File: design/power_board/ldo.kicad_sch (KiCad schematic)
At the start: 10 parts, among them U2 LM317M_DCY

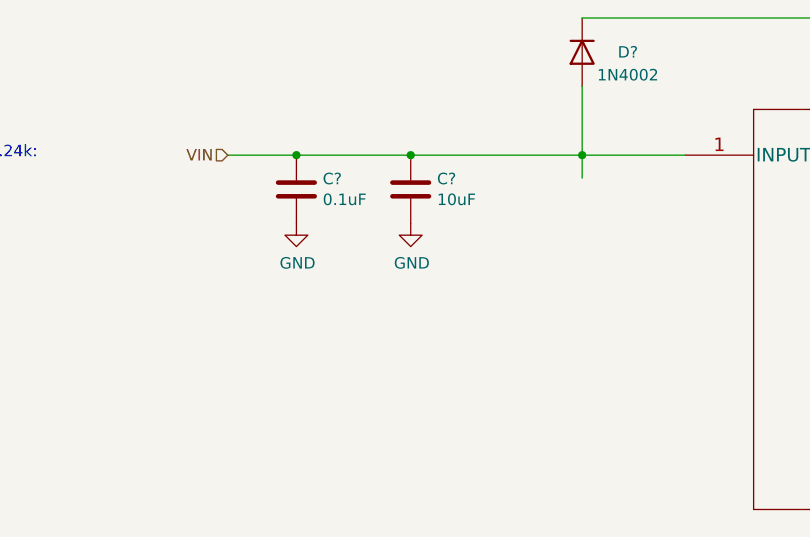
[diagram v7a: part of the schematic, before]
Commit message: Added LED
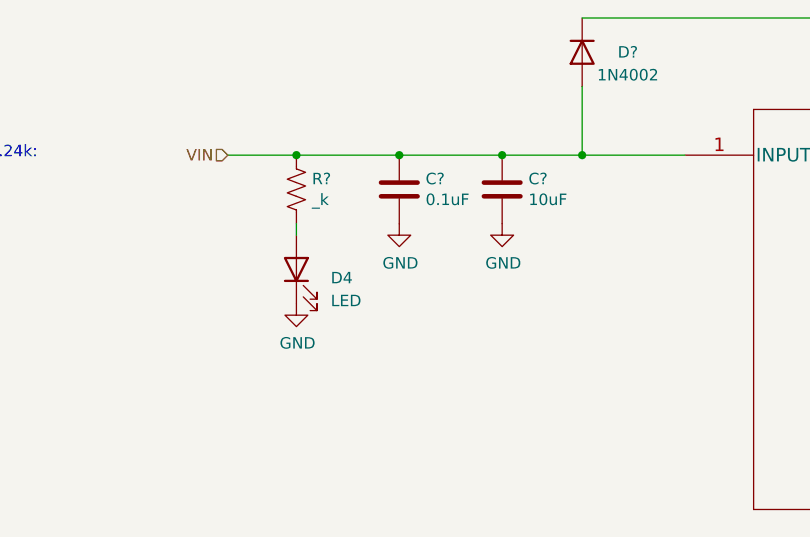
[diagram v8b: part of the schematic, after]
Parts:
- added D4: LED, symbol Device:LED
- added R?: _k, Resistor_SMD:R_0805_2012Metric_Pad1.20x1.40mm_HandSolder, symbol Device:R_US
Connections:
- net GND: now also D4.1 (K)
- net VIN: now also R?.1
- new net: D4.2 (A), R?.2
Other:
- moved on the sheet: C?
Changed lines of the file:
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@@
 (kicad_sch (version 20230121) (generator eeschema)
   (paper "A4")
+  (junction (at 97.79 76.2) (diameter 0) (color 0 0 0 0)
+  )
   (junction (at 224.79 92.71) (diameter 0) (color 0 0 0 0)
   )
   (junction (at 190.5 92.71) (diameter 0) (color 0 0 0 0)
   )
-  (junction (at 97.79 76.2) (diameter 0) (color 0 0 0 0)
+  (junction (at 120.65 76.2) (diameter 0) (color 0 0 0 0)
+  )
+  (junction (at 109.22 76.2) (diameter 0) (color 0 0 0 0)
   )
   (junction (at 190.5 111.76) (diameter 0) (color 0 0 0 0)
@@
   (junction (at 205.74 111.76) (diameter 0) (color 0 0 0 0)
   )
-  (junction (at 110.49 76.2) (diameter 0) (color 0 0 0 0)
-  )
   (junction (at 185.42 111.76) (diameter 0) (color 0 0 0 0)
   )
@@
     (stroke (width 0) (type default))
   )
+  (wire (pts (xy 97.79 76.2) (xy 109.22 76.2))
+    (stroke (width 0) (type default))
+  )
   (wire (pts (xy 129.54 60.96) (xy 198.12 60.96))
     (stroke (width 0) (type default))
@@
     (stroke (width 0) (type default))
   )
-  (wire (pts (xy 129.54 76.2) (xy 110.49 76.2))
+  (wire (pts (xy 129.54 76.2) (xy 120.65 76.2))
+    (stroke (width 0) (type default))
+  )
+  (wire (pts (xy 97.79 83.82) (xy 97.79 85.09))
     (stroke (width 0) (type default))
   )
@@
     (stroke (width 0) (type default))
   )
-  (wire (pts (xy 97.79 76.2) (xy 90.17 76.2))
-    (stroke (width 0) (type default))
-  )
   (wire (pts (xy 185.42 92.71) (xy 190.5 92.71))
     (stroke (width 0) (type default))
@@
     (stroke (width 0) (type default))
   )
-  (wire (pts (xy 110.49 76.2) (xy 97.79 76.2))
+  (wire (pts (xy 90.17 76.2) (xy 97.79 76.2))
     (stroke (width 0) (type default))
   )
@@
     (stroke (width 0) (type default))
   )
-  (wire (pts (xy 129.54 78.74) (xy 129.54 76.2))
+  (wire (pts (xy 109.22 76.2) (xy 120.65 76.2))
     (stroke (width 0) (type default))
   )
@@
     )
   )
-  (symbol (lib_id "Device:C") (at 110.49 80.01 0) (unit 1)
-    (in_bom yes) (on_board yes) (dnp no)
-    (property "Reference" "C?" (at 113.411 78.8416 0)
-      (effects (font (size 1.27 1.27)) (justify left))
-    )
-    (property "Value" "10uF" (at 113.411 81.153 0)
-      (effects (font (size 1.27 1.27)) (justify left))
-    )
-    (property "Footprint" "Capacitor_SMD:C_0805_2012Metric_Pad1.18x1.45mm_HandSolder" (at 111.4552 83.82 0)
-      (effects (font (size 1.27 1.27)) hide)
-    )
-    (property "Datasheet" "~" (at 110.49 80.01 0)
+  (symbol (lib_id "Device:C") (at 120.65 80.01 0) (unit 1)
+    (in_bom yes) (on_board yes) (dnp no)
+    (property "Reference" "C?" (at 123.571 78.8416 0)
+      (effects (font (size 1.27 1.27)) (justify left))
+    )
+    (property "Value" "10uF" (at 123.571 81.153 0)
+      (effects (font (size 1.27 1.27)) (justify left))
+    )
+    (property "Footprint" "Capacitor_SMD:C_0805_2012Metric_Pad1.18x1.45mm_HandSolder" (at 121.6152 83.82 0)
+      (effects (font (size 1.27 1.27)) hide)
+    )
+    (property "Datasheet" "~" (at 120.65 80.01 0)
       (effects (font (size 1.27 1.27)) hide)
     )
@@
     )
   )
+  (symbol (lib_id "Device:R_US") (at 97.79 80.01 0) (unit 1)
+    (in_bom yes) (on_board yes) (dnp no)
+    (property "Reference" "R?" (at 99.5172 78.8416 0)
+      (effects (font (size 1.27 1.27)) (justify left))
+    )
+    (property "Value" "_k" (at 99.5172 81.153 0)
+      (effects (font (size 1.27 1.27)) (justify left))
+    )
+    (property "Footprint" "Resistor_SMD:R_0805_2012Metric_Pad1.20x1.40mm_HandSolder" (at 98.806 80.264 90)
+      (effects (font (size 1.27 1.27)) hide)
+    )
+    (property "Datasheet" "~" (at 97.79 80.01 0)
+      (effects (font (size 1.27 1.27)) hide)
+    )
+    (pin "1")
+    (pin "2")
+    (instances
+      (project "power_board"
+        (path "/8a849c59-59c0-42e0-a511-c33c123656fd"
+          (reference "R?") (unit 1)
+        )
+        (path "/8a849c59-59c0-42e0-a511-c33c123656fd/00000000-0000-0000-0000-00006162a42b"
+          (reference "R10") (unit 1)
+        )
+      )
+      (project "ldo"
+        (path "/d8100ad7-b41c-4ad0-b84d-4686363b20a8"
+          (reference "R9") (unit 1)
+        )
+      )
+    )
+  )
   (symbol (lib_id "power:GND") (at 185.42 123.19 0) (unit 1)
     (in_bom yes) (on_board yes) (dnp no)
@@
     )
   )
-  (symbol (lib_id "Device:C") (at 97.79 80.01 0) (unit 1)
-    (in_bom yes) (on_board yes) (dnp no)
-    (property "Reference" "C?" (at 100.711 78.8416 0)
-      (effects (font (size 1.27 1.27)) (justify left))
-    )
-    (property "Value" "0.1uF" (at 100.711 81.153 0)
-      (effects (font (size 1.27 1.27)) (justify left))
-    )
-    (property "Footprint" "Capacitor_SMD:C_0805_2012Metric_Pad1.18x1.45mm_HandSolder" (at 98.7552 83.82 0)
-      (effects (font (size 1.27 1.27)) hide)
-    )
-    (property "Datasheet" "~" (at 97.79 80.01 0)
+  (symbol (lib_id "Device:C") (at 109.22 80.01 0) (unit 1)
+    (in_bom yes) (on_board yes) (dnp no)
+    (property "Reference" "C?" (at 112.141 78.8416 0)
+      (effects (font (size 1.27 1.27)) (justify left))
+    )
+    (property "Value" "0.1uF" (at 112.141 81.153 0)
+      (effects (font (size 1.27 1.27)) (justify left))
+    )
+    (property "Footprint" "Capacitor_SMD:C_0805_2012Metric_Pad1.18x1.45mm_HandSolder" (at 110.1852 83.82 0)
+      (effects (font (size 1.27 1.27)) hide)
+    )
+    (property "Datasheet" "~" (at 109.22 80.01 0)
       (effects (font (size 1.27 1.27)) hide)
     )
@@
     )
   )
-  (symbol (lib_id "power:GND") (at 97.79 83.82 0) (unit 1)
-    (in_bom yes) (on_board yes) (dnp no)
-    (property "Reference" "#PWR?" (at 97.79 90.17 0)
-      (effects (font (size 1.27 1.27)) hide)
-    )
-    (property "Value" "GND" (at 97.917 88.2142 0)
-      (effects (font (size 1.27 1.27)))
-    )
-    (property "Footprint" "" (at 97.79 83.82 0)
-      (effects (font (size 1.27 1.27)) hide)
-    )
-    (property "Datasheet" "" (at 97.79 83.82 0)
+  (symbol (lib_id "power:GND") (at 109.22 83.82 0) (unit 1)
+    (in_bom yes) (on_board yes) (dnp no)
+    (property "Reference" "#PWR?" (at 109.22 90.17 0)
+      (effects (font (size 1.27 1.27)) hide)
+    )
+    (property "Value" "GND" (at 109.347 88.2142 0)
+      (effects (font (size 1.27 1.27)))
+    )
+    (property "Footprint" "" (at 109.22 83.82 0)
+      (effects (font (size 1.27 1.27)) hide)
+    )
+    (property "Datasheet" "" (at 109.22 83.82 0)
       (effects (font (size 1.27 1.27)) hide)
     )
@@
     )
   )
+  (symbol (lib_id "power:GND") (at 97.79 92.71 0) (unit 1)
+    (in_bom yes) (on_board yes) (dnp no)
+    (property "Reference" "#PWR?" (at 97.79 99.06 0)
+      (effects (font (size 1.27 1.27)) hide)
+    )
+    (property "Value" "GND" (at 97.917 97.1042 0)
+      (effects (font (size 1.27 1.27)))
+    )
+    (property "Footprint" "" (at 97.79 92.71 0)
+      (effects (font (size 1.27 1.27)) hide)
+    )
+    (property "Datasheet" "" (at 97.79 92.71 0)
+      (effects (font (size 1.27 1.27)) hide)
+    )
+    (pin "1")
+    (instances
+      (project "power_board"
+        (path "/8a849c59-59c0-42e0-a511-c33c123656fd"
+          (reference "#PWR?") (unit 1)
+        )
+        (path "/8a849c59-59c0-42e0-a511-c33c123656fd/00000000-0000-0000-0000-00006162a42b"
+          (reference "#PWR022") (unit 1)
+        )
+      )
+      (project "ldo"
+        (path "/d8100ad7-b41c-4ad0-b84d-4686363b20a8"
+          (reference "#PWR0102") (unit 1)
+        )
+      )
+    )
+  )
   (symbol (lib_id "Device:R_US") (at 190.5 101.6 180) (unit 1)
     (in_bom yes) (on_board yes) (dnp no)
@@
     )
   )
-  (symbol (lib_id "power:GND") (at 110.49 83.82 0) (unit 1)
-    (in_bom yes) (on_board yes) (dnp no)
-    (property "Reference" "#PWR?" (at 110.49 90.17 0)
-      (effects (font (size 1.27 1.27)) hide)
-    )
-    (property "Value" "GND" (at 110.617 88.2142 0)
-      (effects (font (size 1.27 1.27)))
-    )
-    (property "Footprint" "" (at 110.49 83.82 0)
-      (effects (font (size 1.27 1.27)) hide)
-    )
-    (property "Datasheet" "" (at 110.49 83.82 0)
-      (effects (font (size 1.27 1.27)) hide)
-    )
+  (symbol (lib_id "Device:LED") (at 97.79 88.9 90) (unit 1)
+    (in_bom yes) (on_board yes) (dnp no) (fields_autoplaced)
+    (property "Reference" "D4" (at 101.6 89.8525 90)
+      (effects (font (size 1.27 1.27)) (justify right))
+    )
+    (property "Value" "LED" (at 101.6 92.3925 90)
+      (effects (font (size 1.27 1.27)) (justify right))
+    )
+    (property "Footprint" "" (at 97.79 88.9 0)
+      (effects (font (size 1.27 1.27)) hide)
+    )
+    (property "Datasheet" "~" (at 97.79 88.9 0)
+      (effects (font (size 1.27 1.27)) hide)
+    )
+    (pin "1")
+    (pin "2")
+    (instances
+      (project "power_board"
+        (path "/8a849c59-59c0-42e0-a511-c33c123656fd/00000000-0000-0000-0000-00006162a42b"
+          (reference "D4") (unit 1)
+        )
+      )
+    )
+  )
+  (symbol (lib_id "power:GND") (at 120.65 83.82 0) (unit 1)
+    (in_bom yes) (on_board yes) (dnp no)
+    (property "Reference" "#PWR?" (at 120.65 90.17 0)
+      (effects (font (size 1.27 1.27)) hide)
+    )
+    (property "Value" "GND" (at 120.777 88.2142 0)
+      (effects (font (size 1.27 1.27)))
+    )
+    (property "Footprint" "" (at 120.65 83.82 0)
+      (effects (font (size 1.27 1.27)) hide)
+    )
+    (property "Datasheet" "" (at 120.65 83.82 0)
+      (effects (font (size 1.27 1.27)) hide)
+    )
